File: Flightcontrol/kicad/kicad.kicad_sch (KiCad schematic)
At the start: 16 parts, among them J1 2171790001, J2 Conn_01x03_Pin, J3 Conn_01x03_Pin, U1 ESP32-S3-WROOM-1U-N16R8

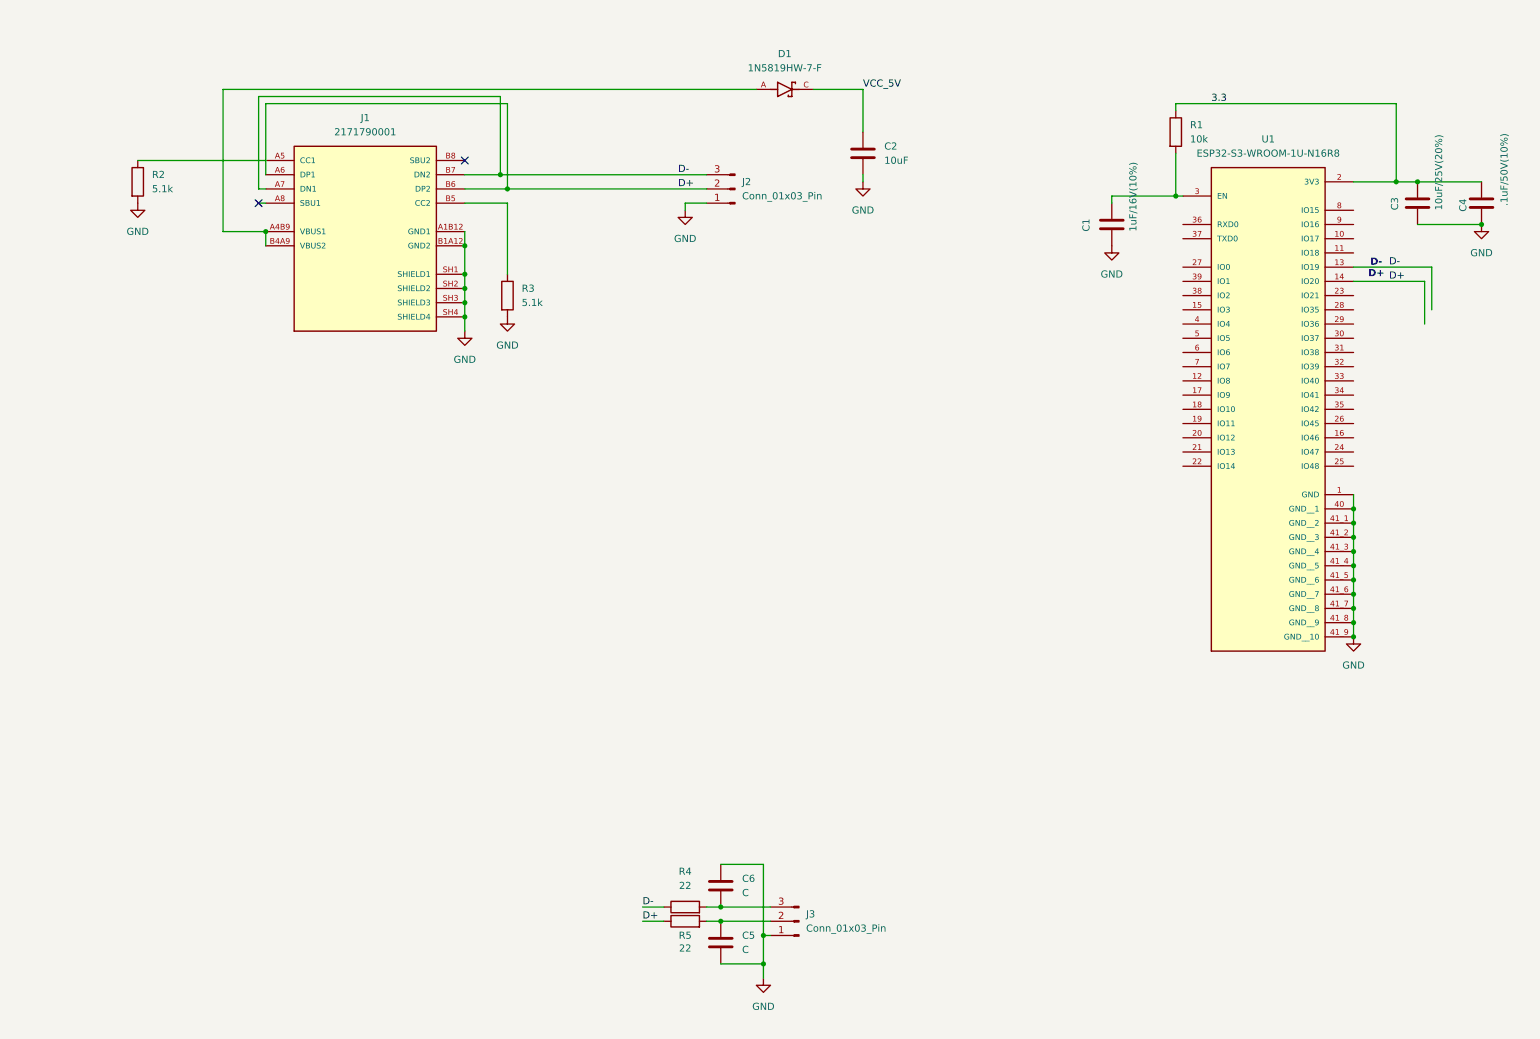
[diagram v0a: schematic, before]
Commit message: flasher4otg V1 finished
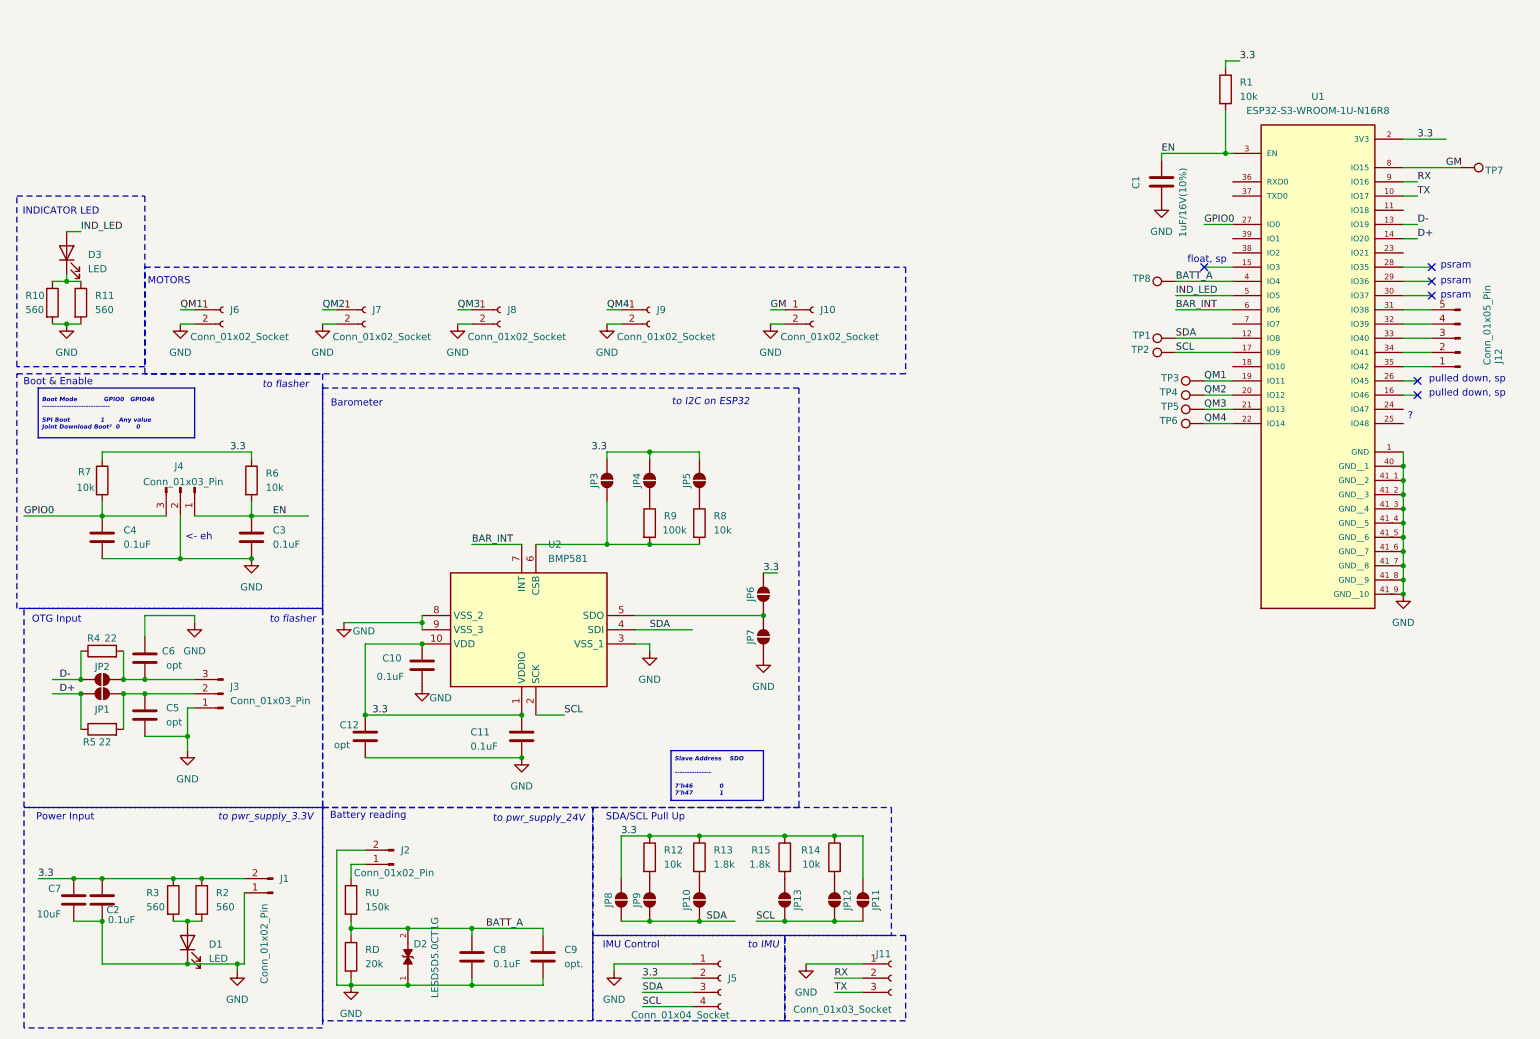
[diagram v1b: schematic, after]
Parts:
- removed D1: 1N5819HW-7-F, 1N5819HW-7-F:SOD3715X145N, symbol 1N5819HW-7-F:1N5819HW-7-F
- removed J1: 2171790001, 2171790001:MOLEX_2171790001, symbol 2171790001:2171790001
- removed J2: Conn_01x03_Pin, symbol Connector:Conn_01x03_Pin
- added C10, C11, C8: 0.1uF, symbol Device:C
- added C12: opt, Capacitor_SMD:C_0603_1608Metric, symbol Device:C
- added C7: 10uF, Capacitor_SMD:C_0603_1608Metric, symbol Device:C
- added C9: opt., symbol Device:C
- added D1: LED, LED_SMD:LED_0201_0603Metric, symbol Device:LED
- added D2: LESD5D5.0CT1G, LESD5D5.0CT1G:TVS_LESD5D5.0CT1G, symbol LESD5D5.0CT1G:LESD5D5.0CT1G
- added D3: LED, symbol Device:LED
- added J1, J2: Conn_01x02_Pin, symbol Connector:Conn_01x02_Pin
- added J10, J6, J7, J8, J9: Conn_01x02_Socket, symbol Connector:Conn_01x02_Socket
- added J11: Conn_01x03_Socket, symbol Connector:Conn_01x03_Socket
- added J12: Conn_01x05_Pin, symbol Connector:Conn_01x05_Pin
- added J4: Conn_01x03_Pin, symbol Connector:Conn_01x03_Pin
- added J5: Conn_01x04_Socket, CONN_CCSH-W10R-04TR-BK-A_ADA:CONN_CCSH-W10R-04TR-BK-A_ADA, symbol Connector:Conn_01x04_Socket
- added JP1, JP10, JP11, JP12, JP13, JP2, JP3, JP4, JP5, JP6, JP7, JP8, JP9: SolderJumper_2_Open, Jumper:SolderJumper-2_P1.3mm_Open_RoundedPad1.0x1.5mm, symbol Jumper:SolderJumper_2_Open
- added R10, R11: 560, Resistor_SMD:R_0805_2012Metric, symbol Device:R
- added R12, R14, R6, R7, R8: 10k, symbol Device:R
- added R13, R15: 1.8k, symbol Device:R
- added R9: 100k, symbol Device:R
- added RD: 20k, symbol Device:R
- added RU: 150k, symbol Device:R
- added TP1, TP3, TP5, TP7, TP8: x, TestPoint:TestPoint_Pad_D1.5mm, symbol Connector:TestPoint
- added TP2, TP4, TP6: BAR_CLK, TestPoint:TestPoint_Pad_D1.5mm, symbol Connector:TestPoint
- added U2: BMP581, BMP581:BMP581, symbol BMP581:BMP581
- C2: value 10uF -> 0.1uF; footprint (none) -> Capacitor_SMD:C_0603_1608Metric
- C3: value 10uF/25V(20%) -> 0.1uF; footprint (none) -> Capacitor_SMD:C_0603_1608Metric
- C4: value .1uF/50V(10%) -> 0.1uF; footprint (none) -> Capacitor_SMD:C_0603_1608Metric
- C5, C6: value C -> opt; footprint (none) -> Capacitor_SMD:C_0603_1608Metric
- R2, R3: value 5.1k -> 560; footprint (none) -> Resistor_SMD:R_0805_2012Metric
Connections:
- net VCC_5V is gone; now on net 3.3: C2.1
- net 3.3: now also R2.1, R3.1, C10.1, C11.1, C12.1, C7.1, J1.2 (Pin_2), J5.2 (Pin_2), JP11.2 (B), JP3.2 (B), JP4.2 (B), JP5.2 (B), JP6.2 (B), JP8.2 (B), R12.1, R13.1, R14.1, R15.1, R6.1, R7.1, U2.1 (VDDIO), U2.10 (VDD); no longer C3.1, C4.1
- net D+: now also JP1.1 (A)
- net D-: now also JP2.1 (A)
- net GND: now also C10.2, C11.2, C12.2, C7.2, C8.2, C9.2, D1.1 (K), D2.1, J1.1 (Pin_1), J10.2 (Pin_2), J11.1 (Pin_1), J2.2 (Pin_2), J4.2 (Pin_2), J5.1 (Pin_1), J6.2 (Pin_2), J7.2 (Pin_2), J8.2 (Pin_2), J9.2 (Pin_2), JP7.1 (A), R10.2, R11.2, RD.2, U2.3 (VSS_1), U2.8 (VSS_2), U2.9 (VSS_3); no longer R2.2, R3.2
- net at C6.2, J3.3 (Pin_3), R4.2: now also JP2.2 (B)
- net at C5.1, J3.2 (Pin_2), R5.2: now also JP1.2 (B)
- net EN: now reaches C1.1, R1.2, U1.3 (EN)
- net EN: now also C3.1, J4.1 (Pin_1), R6.2
- net TX: now reaches U1.10 (IO17)
- net TX: now also J11.3 (Pin_3)
- net SDA: now reaches U1.12 (IO8)
- net SDA: now also J5.3 (Pin_3), JP10.1 (A), JP8.1 (A), JP9.1 (A), TP1.1, U2.4 (SDI)
- net SCL: now reaches U1.17 (IO9)
- net SCL: now also J5.4 (Pin_4), JP11.1 (A), JP12.1 (A), JP13.1 (A), TP2.1, U2.2 (SCK)
- net QM1: now reaches U1.19 (IO11)
- net QM1: now also J6.1 (Pin_1), TP3.1
- net QM2: now reaches U1.20 (IO12)
- net QM2: now also J7.1 (Pin_1), TP4.1
- net QM3: now reaches U1.21 (IO13)
- net QM3: now also J8.1 (Pin_1), TP5.1
- net QM4: now reaches U1.22 (IO14)
- net QM4: now also J9.1 (Pin_1), TP6.1
- net GPIO0: now reaches U1.27 (IO0)
- net GPIO0: now also C4.1, J4.3 (Pin_3), R7.2
- net at U1.31 (IO38): now also J12.5 (Pin_5)
- net at U1.32 (IO39): now also J12.4 (Pin_4)
- net at U1.33 (IO40): now also J12.3 (Pin_3)
- net at U1.34 (IO41): now also J12.2 (Pin_2)
- net at U1.35 (IO42): now also J12.1 (Pin_1)
- net BATT_A: now reaches U1.4 (IO4)
- net BATT_A: now also C8.1, C9.1, D2.2, RD.1, RU.2, TP8.1
- net IND_LED: now reaches U1.5 (IO5)
- net IND_LED: now also D3.2 (A)
- net BAR_INT: now reaches U1.6 (IO6)
- net BAR_INT: now also U2.7 (INT)
- net GM: now reaches U1.8 (IO15)
- net GM: now also J10.1 (Pin_1), TP7.1
- net RX: now reaches U1.9 (IO16)
- net RX: now also J11.2 (Pin_2)
- new net: JP9.2 (B), R12.2
- new net: D1.2 (A), R2.2, R3.2
- new net: JP4.1 (A), R9.1
- new net: JP3.1 (A), R8.2, R9.2, U2.6 (CSB)
- new net: JP13.2 (B), R15.2
- new net: JP10.2 (B), R13.2
- new net: JP12.2 (B), R14.2
- new net: J2.1 (Pin_1), RU.1
- new net: D3.1 (K), R10.1, R11.1
- new net: JP6.1 (A), JP7.2 (B), U2.5 (SDO)
- new net: JP5.1 (A), R8.1
- no-connect marks 2 -> 6
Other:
- note added: "<- eh"
- note added: "?"
- note added: "Barometer"
- note added: "Battery reading"
- note added: "Boot & Enable"
- note added: "IMU Control"
- note added: "INDICATOR LED"
- note added: "MOTORS"
- note added: "OTG Input"
- note added: "Power Input"
- note added: "SDA/SCL Pull Up"
- note added: "float, sp"
- note added: "psram"
- note added: "pulled down, sp"
- note added: "to I2C on ESP32"
- note added: "to IMU"
- note added: "to flasher"
- note added: "to pwr_supply_24V"
- note added: "to pwr_supply_3.3V"
- note removed: "D- D+"
- moved on the sheet: C1, C5, C6, J3, R1, R4, R5, U1

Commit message: finished main schematic
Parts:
- removed J1, J2: Conn_01x02_Pin, symbol Connector:Conn_01x02_Pin
- removed J10, J6, J7, J8, J9: Conn_01x02_Socket, symbol Connector:Conn_01x02_Socket
- removed J3: Conn_01x03_Pin, symbol Connector:Conn_01x03_Pin
- added J1: Conn_01x03_Pin, CONN_SM03B-GHS-TBLFSN_JST:CONN_SM03B-GHS-TBLFSN_JST, symbol Connector:Conn_01x03_Pin
- added J2: Conn_01x06_Socket, CONN_SM06B-GHS-TB_JST:CONN_SM06B-GHS-TB_JST, symbol Connector:Conn_01x06_Socket
- added J6: Conn_01x01_Pin, Connector_PinHeader_2.54mm:PinHeader_1x01_P2.54mm_Vertical, symbol Connector:Conn_01x01_Pin
- C1, C10, C11, C8, C9: footprint (none) -> Capacitor_SMD:C_0603_1608Metric
- D3: footprint (none) -> LED_SMD:LED_0603_1608Metric
- J11: footprint (none) -> CONN_SM03B-GHS-TBLFSN_JST:CONN_SM03B-GHS-TBLFSN_JST
- J4: footprint (none) -> Connector_PinHeader_2.54mm:PinHeader_1x03_P2.54mm_Vertical
- R1, R12, R13, R14, R15, R4, R5, R6, R7, R8, R9, RU: footprint (none) -> Resistor_SMD:R_0603_1608Metric
- RD: footprint (none) -> Resistor_SMD:R_0805_2012Metric
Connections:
- net 3.3: now also J1.3 (Pin_3)
- net GM: now also J2.6 (Pin_6)
- net GND: now also J1.2 (Pin_2), J2.1 (Pin_1); no longer J4.2 (Pin_2)
- net GPIO0: now also J6.1 (Pin_1); no longer J4.3 (Pin_3)
- net QM1: now also J2.2 (Pin_2)
- net QM2: now also J2.3 (Pin_3)
- net QM3: now also J2.4 (Pin_4)
- net QM4: now also J2.5 (Pin_5)
- net at C6.2, JP2.2 (B), R4.2: now also J4.3 (Pin_3)
- net at C5.1, JP1.2 (B), R5.2: now also J4.2 (Pin_2)
- net at RU.1: now also J1.1 (Pin_1)
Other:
- note added: "TRANSCEIVER"
- note removed: "<- eh"
- moved on the sheet: C5, C6, D3, J11, J5, JP1, JP2, R10, R11, R4, R5

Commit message: backing up for personal reasons
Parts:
- removed J1: Conn_01x03_Pin, CONN_SM03B-GHS-TBLFSN_JST:CONN_SM03B-GHS-TBLFSN_JST, symbol Connector:Conn_01x03_Pin
- removed J11: Conn_01x03_Socket, CONN_SM03B-GHS-TBLFSN_JST:CONN_SM03B-GHS-TBLFSN_JST, symbol Connector:Conn_01x03_Socket
- removed J2: Conn_01x06_Socket, CONN_SM06B-GHS-TB_JST:CONN_SM06B-GHS-TB_JST, symbol Connector:Conn_01x06_Socket
- removed J5: Conn_01x04_Socket, CONN_CCSH-W10R-04TR-BK-A_ADA:CONN_CCSH-W10R-04TR-BK-A_ADA, symbol Connector:Conn_01x04_Socket
- removed JP12, JP13, JP4, JP7: SolderJumper_2_Open, Jumper:SolderJumper-2_P1.3mm_Open_RoundedPad1.0x1.5mm, symbol Jumper:SolderJumper_2_Open
- added J2: Conn_01x06, CONN_CCSH-W10R-04TR-BK-A_ADA:CONN_CCSH-W10R-04TR-BK-A_ADA, symbol Connector_Generic:Conn_01x06
- added J3: Conn_01x08, CONN_SM06B-GHS-TB_JST:CONN_SM06B-GHS-TB_JST, symbol Connector_Generic:Conn_01x08
- added J5, J7: Conn_01x05, CONN_SM03B-GHS-TBLFSN_JST:CONN_SM03B-GHS-TBLFSN_JST, symbol Connector_Generic:Conn_01x05
- added JP14: SolderJumper_2_Open, Jumper:SolderJumper-2_P1.3mm_Open_RoundedPad1.0x1.5mm, symbol Jumper:SolderJumper_2_Open
- added R16: 10, Resistor_SMD:R_0603_1608Metric, symbol Device:R
- J12: footprint (none) -> Connector_PinHeader_2.54mm:PinHeader_1x05_P2.54mm_Vertical
- R8: value 10k -> 10
- U1: footprint ESP32-S3-WROOM-1U-N16R8:XCVR_ESP32-S3-WROOM-1U-N16R8 -> RF_Module:ESP32-S3-WROOM-1U
- renumbered RD to RD1, RU to RU1
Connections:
- net 3.3: now also R8.1, J2.2 (Pin_2), J7.1 (Pin_1), JP14.2 (B), R16.1; no longer C10.1, C11.1, JP11.2 (B), JP6.2 (B), JP8.2 (B), U2.1 (VDDIO), U2.10 (VDD)
- net D+: now also JP1.2 (B); no longer JP1.1 (A)
- net D-: now also JP2.2 (B); no longer JP2.1 (A)
- net GM: now also J3.6 (Pin_6)
- net GND: now also JP6.1 (A), J2.1 (Pin_1), J3.1 (Pin_1), J5.1 (Pin_1), J7.2 (Pin_2)
- net QM1: now also J3.2 (Pin_2)
- net QM2: now also J3.3 (Pin_3)
- net QM3: now also J3.4 (Pin_4)
- net QM4: now also J3.5 (Pin_5)
- net RX: now also J5.2 (Pin_2)
- net SCL: now also JP10.1 (A), J2.4 (Pin_4)
- net SDA: now also J2.3 (Pin_3); no longer JP10.1 (A)
- net TX: now also J5.3 (Pin_3)
- net at R12.2: now also JP8.2 (B); no longer JP9.2 (B)
- net DN: now reaches C6.2, J4.3 (Pin_3), R4.2
- net DN: now also JP2.1 (A); no longer JP2.2 (B)
- net at R9.1: now also JP3.1 (A)
- net at R9.2, U2.6 (CSB): now also JP14.1 (A); no longer JP3.1 (A), R8.2
- net at R15.2: now also JP10.2 (B)
- net DP: now reaches C5.1, J4.2 (Pin_2), R5.2
- net DP: now also JP1.1 (A); no longer JP1.2 (B)
- net at R13.2: now also JP9.2 (B); no longer JP10.2 (B)
- net VBAT: now reaches RU1.1
- net VBAT: now also J7.3 (Pin_3)
- net at R14.2: now also JP11.2 (B)
- net at U2.5 (SDO): now also JP5.1 (A), JP6.2 (B); no longer JP6.1 (A)
- new net: C11.1, R8.2, U2.1 (VDDIO)
- new net: C10.1, R16.2, U2.10 (VDD)
- no-connect marks 6 -> 24
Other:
- note added: "<- 10k?"
- note added: "X"

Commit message: sanity backup
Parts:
- removed J4: Conn_01x03_Pin, Connector_PinHeader_2.54mm:PinHeader_1x03_P2.54mm_Vertical, symbol Connector:Conn_01x03_Pin
- removed J6: Conn_01x01_Pin, Connector_PinHeader_2.54mm:PinHeader_1x01_P2.54mm_Vertical, symbol Connector:Conn_01x01_Pin
- removed JP1, JP10, JP11, JP14, JP2, JP3, JP8, JP9: SolderJumper_2_Open, Jumper:SolderJumper-2_P1.3mm_Open_RoundedPad1.0x1.5mm, symbol Jumper:SolderJumper_2_Open
- removed R13, R15: 1.8k, Resistor_SMD:R_0603_1608Metric, symbol Device:R
- added J1: Conn_01x04_Pin, Connector_PinHeader_2.54mm:PinHeader_1x04_P2.54mm_Vertical, symbol Connector:Conn_01x04_Pin
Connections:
- net 3.3: now also R9.1
- net BAR_INT: now also U1.12 (IO8); no longer U1.6 (IO6)
- net DN: now also J1.3 (Pin_3)
- net DP: now also J1.2 (Pin_2)
- net EN: now also J1.1 (Pin_1)
- net GM: now also U1.23 (IO21); no longer U1.8 (IO15)
- net GPIO0: now also J1.4 (Pin_4)
- net RX: now also U1.38 (IO2); no longer U1.9 (IO16)
- net SCL: now also R14.2, TP1.1, U1.9 (IO16); no longer TP2.1, U1.17 (IO9)
- net SDA: now also R12.2, TP2.1, U1.8 (IO15); no longer TP1.1, U1.12 (IO8)
- net TX: now also U1.39 (IO1); no longer U1.10 (IO17)
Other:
- moved on the sheet: R12, R14, TP1, TP2, TP7

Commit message: FC.V1 PCB Layout completed
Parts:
- removed J12: Conn_01x05_Pin, Connector_PinHeader_2.54mm:PinHeader_1x05_P2.54mm_Vertical, symbol Connector:Conn_01x05_Pin
- removed TP1: x, TestPoint:TestPoint_Pad_D1.5mm, symbol Connector:TestPoint
- removed TP2: BAR_CLK, TestPoint:TestPoint_Pad_D1.5mm, symbol Connector:TestPoint
- added H1, H2, H3, H4: MountingHole, MountingHole:MountingHole_2.2mm_M2, symbol Mechanical:MountingHole
- added J4: Conn_01x01_Pin, Connector_PinHeader_2.54mm:PinHeader_1x01_P2.54mm_Vertical, symbol Connector:Conn_01x01_Pin
- added J6: Conn_01x03_Pin, Connector_PinHeader_2.54mm:PinHeader_1x03_P2.54mm_Vertical, symbol Connector:Conn_01x03_Pin
- D1: footprint LED_SMD:LED_0201_0603Metric -> LED_SMD:LED_0603_1608Metric
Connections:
- net GND: now also J4.1 (Pin_1)
- net IND_LED: now also U1.31 (IO38); no longer U1.5 (IO5)
- net at U1.34 (IO41): now also J6.1 (Pin_1)
- net at U1.33 (IO40): now also J6.2 (Pin_2)
- net at U1.32 (IO39): now also J6.3 (Pin_3)
- no-connect marks 24 -> 26
